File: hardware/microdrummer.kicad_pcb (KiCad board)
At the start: 2 copper layers, 19 x 106.5 mm, 15 parts, among them J1 Thonk, J2 Thonk, J3 Thonk, SW1 SW_SPST, SW2 SW_SPST, U1 Teensy3.2

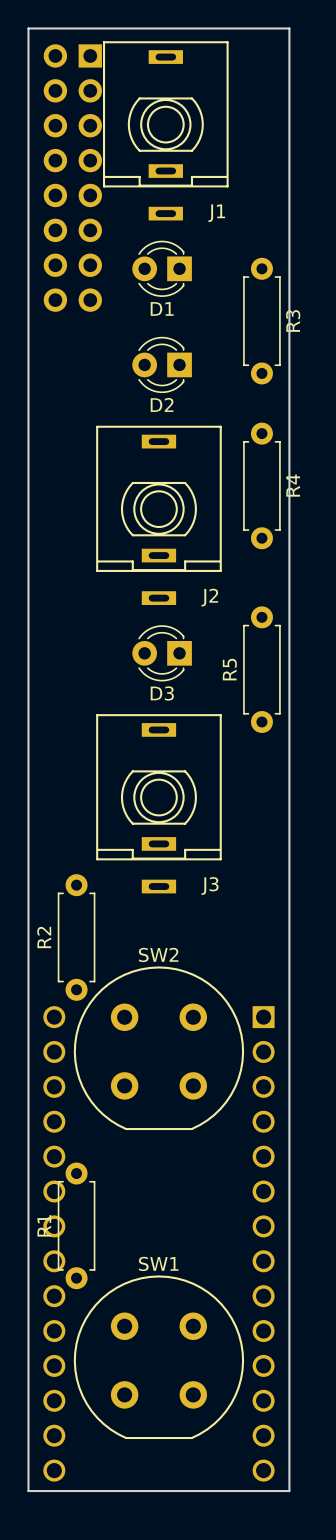
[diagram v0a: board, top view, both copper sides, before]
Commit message: Laid out PCB
I had to move some of the pins around.
I still need to update the code to match.
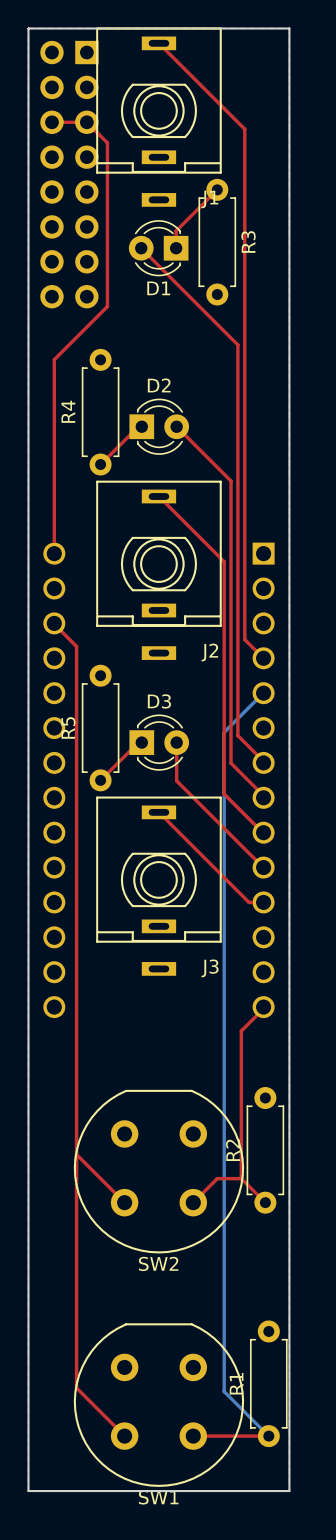
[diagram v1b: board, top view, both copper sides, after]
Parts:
- moved U1 33.8 mm to (146.5, 92.8)
- moved R2 20.7 mm to (154.2, 123.5)
- moved R1 18.1 mm to (154.5, 140.5)
- moved SW2 14.4 mm to (149.0, 123.5), turned to 180 degrees
- moved R5 12.5 mm to (142.2, 92.8)
- moved R4 12.0 mm to (142.2, 69.8), turned to 90 degrees
- moved SW1 9.43 mm to (149.0, 140.5), turned to 180 degrees
- moved D3 7.06 mm to (145.2, 90.0), turned to 0 degrees
- moved R3 6.60 mm to (150.8, 49.8)
- moved J3 6.00 mm to (146.5, 100.0)
- moved D2 5.27 mm to (145.2, 67.0), turned to 0 degrees
- moved J2 4.00 mm to (146.5, 77.0)
- moved D1 1.52 mm to (147.8, 54.0)
- moved J1 1.12 mm to (146.5, 44.0)
- moved H1 0.35 mm to (141.2, 39.8)
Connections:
- U1 pad 14: (no net) -> Net-(R2-Pad1)
- U1 pad 31: (no net) -> Net-(SW1-Pad2)
- U1 pad 6: Net-(R2-Pad1) -> (no net)
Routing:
- net Net-(SW1-Pad2): track 0.00 -> 66.3 mm
- net Net-(R1-Pad1): track 0.00 -> 62.1 mm
- net Net-(J1-Pad3): track 0.00 -> 47.9 mm
- net Net-(D1-Pad2): track 0.00 -> 41.2 mm
- net Net-(H1-Pad5): track 0.00 -> 36.7 mm
- net Net-(D2-Pad2): track 0.00 -> 29.6 mm
- net Net-(J2-Pad3): track 0.00 -> 27.7 mm
- net Net-(R2-Pad1): track 0.00 -> 19.9 mm
- net Net-(D3-Pad2): track 0.00 -> 11.7 mm
- net Net-(J3-Pad3): track 0.00 -> 10.3 mm
- net Net-(D1-Pad1): track 0.00 -> 5.49 mm
- net Net-(D3-Pad1): track 0.00 -> 4.14 mm
- net Net-(D2-Pad1): track 0.00 -> 4.14 mm
- added copper zone on B.Cu, net Net-(H1-Pad10)
- added copper zone on F.Cu, net Net-(H1-Pad10)
